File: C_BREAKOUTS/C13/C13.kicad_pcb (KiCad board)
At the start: 2 copper layers, 48.3 x 27.9 mm, 9 parts, among them J0 Conn_01x01_Male, J1 Conn_01x01_Male, J2 Conn_01x09_Female, J3 Conn_01x09_Female, J4 Conn_02x09_Odd_Even

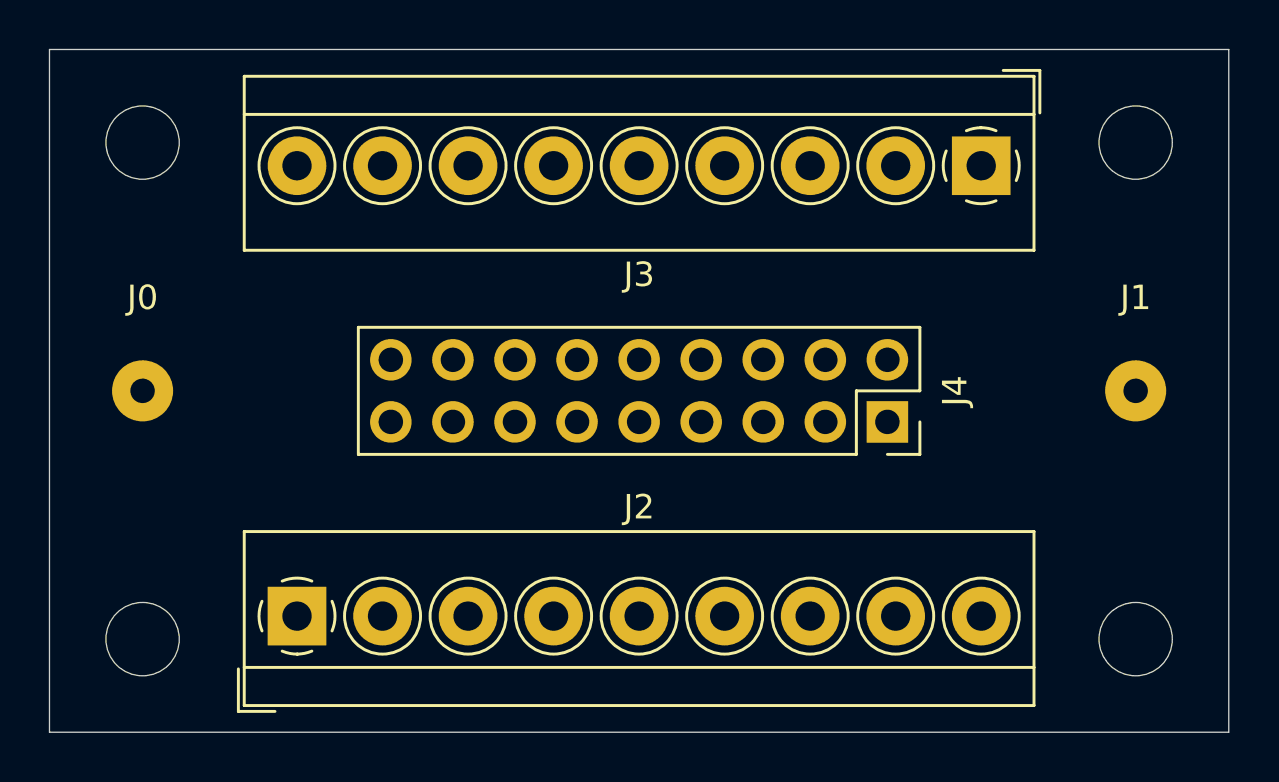
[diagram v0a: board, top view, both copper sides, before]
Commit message: all traces routed
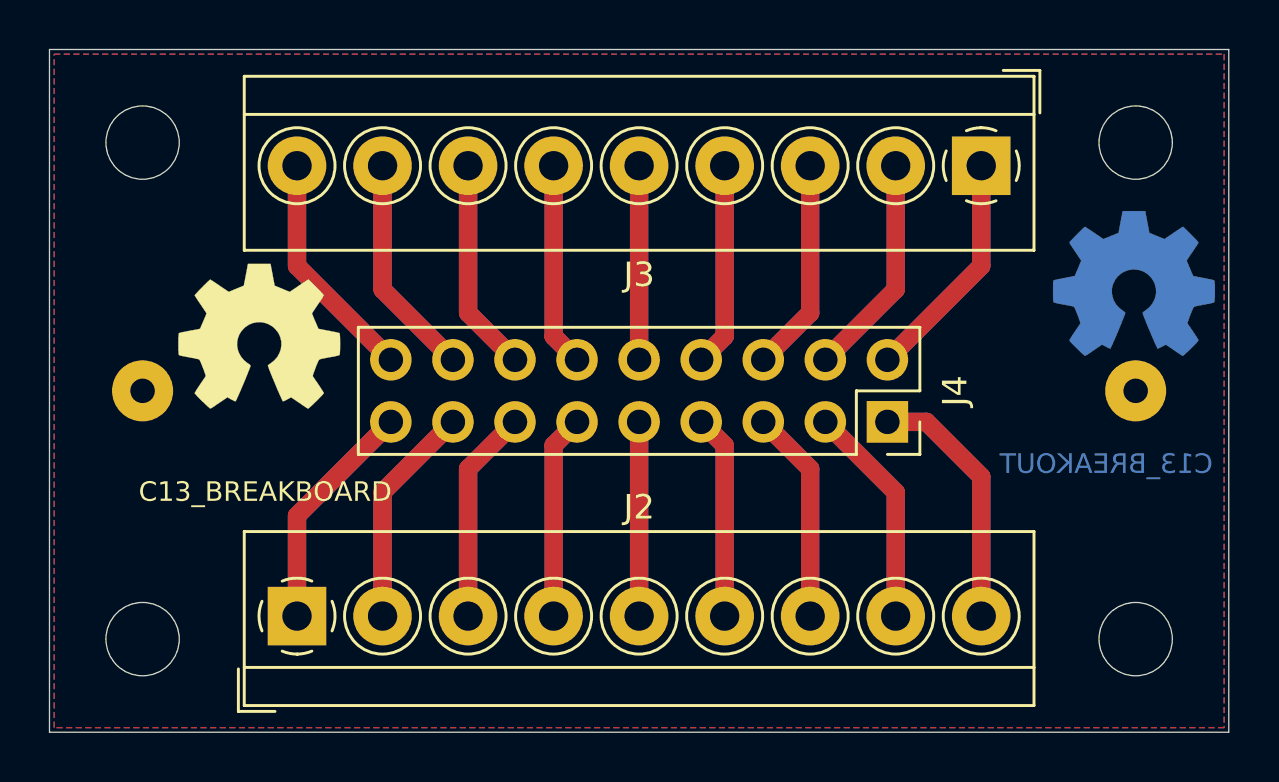
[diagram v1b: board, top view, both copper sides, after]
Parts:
- added REF**: OSHW-Symbol_6.7x6mm_Copper, Symbol:OSHW-Symbol_6.7x6mm_Copper, B.Cu at (64.4, 29.6)
- added REF**: OSHW-Symbol_6.7x6mm_SilkScreen, Symbol:OSHW-Symbol_6.7x6mm_SilkScreen, F.Cu at (28.6, 31.8)
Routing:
- net Net-(J2-Pad9): track 0.00 -> 21.0 mm
- net Net-(J2-Pad1): track 0.00 -> 19.1 mm
- net Net-(J3-Pad1): track 0.00 -> 19.1 mm
- net Net-(J3-Pad9): track 0.00 -> 19.1 mm
- net Net-(J2-Pad8): track 0.00 -> 18.3 mm
- net Net-(J2-Pad2): track 0.00 -> 18.3 mm
- net Net-(J3-Pad2): track 0.00 -> 18.3 mm
- net Net-(J3-Pad8): track 0.00 -> 18.3 mm
- net Net-(J2-Pad7): track 0.00 -> 17.5 mm
- net Net-(J2-Pad3): track 0.00 -> 17.5 mm
- net Net-(J3-Pad3): track 0.00 -> 17.5 mm
- net Net-(J3-Pad7): track 0.00 -> 17.5 mm
- net Net-(J2-Pad6): track 0.00 -> 16.7 mm
- net Net-(J2-Pad4): track 0.00 -> 16.7 mm
- net Net-(J3-Pad6): track 0.00 -> 16.7 mm
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- added copper zone on B.Cu, net Net-(J0-Pad1)
- added copper zone on F.Cu, net Net-(J0-Pad1)
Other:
- net class Default: trace_width 0.25 -> 0.75
- board text added: "C13_BREAKBOARD"
- board text added: "C13_BREAKOUT"
